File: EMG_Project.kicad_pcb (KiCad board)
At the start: 2 copper layers, 78 parts, among them J1 Conn_01x03, J10 Conn_01x01, J11 Conn_01x01, J12 Conn_01x02, J13 Conn_01x01, J14 Conn_01x01, J15 Conn_01x01, J16 Conn_01x01, J17 Conn_01x03, J2 Conn_01x06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

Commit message: First layout sketch
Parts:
- removed J13, J16, J3: Conn_01x01, Connector_PinHeader_2.54mm:PinHeader_1x01_P2.54mm_Vertical
- added J18: Conn_01x02, Connector_PinHeader_2.54mm:PinHeader_1x02_P2.54mm_Horizontal, F.Cu at (66.9, 57.1)
- added R26: 0, Resistor_SMD:R_0603_1608Metric_Pad0.98x0.95mm_HandSolder, F.Cu at (100.5, 65.2)
- U1: footprint EMG Projct Footprints:MP2322GQHZ -> EMG Projct Footprints:QFN-8_1p5MMx2MM_MNP
- moved H3 132.2 mm to (150.8, 66.0)
- moved H2 129.9 mm to (150.8, 44.1)
- moved C10 97.0 mm to (144.6, 43.5)
- moved C11 93.5 mm to (144.6, 46.5)
- moved J11 92.4 mm to (72.0, 57.0)
- moved C19 90.7 mm to (143.2, 52.0), turned to -90 degrees
- moved C20 88.3 mm to (140.0, 65.1), turned to 90 degrees
- moved C12 87.6 mm to (136.7, 57.5), turned to -90 degrees
- moved J14 86.9 mm to (85.7, 65.4)
- moved R17 82.9 mm to (143.2, 65.1), turned to -90 degrees
- moved C17 80.5 mm to (131.3, 62.4), turned to 180 degrees
- moved R16 79.8 mm to (140.7, 43.5), turned to 180 degrees
- moved R12 79.7 mm to (140.7, 46.5), turned to 180 degrees
- moved R23 79.0 mm to (143.2, 57.5), turned to -90 degrees
- moved R19 78.0 mm to (136.7, 65.1), turned to 90 degrees
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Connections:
- J1 pad 1: /REG_OUT -> +5V
- J1 pad 3: +5V -> /REG_OUT
- U2 pad 2: /V_OUT_SENSOR -> /V_IN_MCU
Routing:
- added copper zone on In2.Cu, net +3.3V
- added copper zone on In2.Cu, net /V_REF
- added copper zone on B.Cu, net GND
- added copper zone on In1.Cu, net GND
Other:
- board outline added: 97.1 x 32.3 mm
- copper layers 2 -> 4
- board text added: "+5V"
- board text added: "AAOO"
- board text added: "GND"
- board text added: "MISO"
- board text added: "MOSI"
- board text added: "Power ON"
- board text added: "R"
- board text added: "RST"
- board text added: "S"
- board text added: "SCK"
- board text added: "T"

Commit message: Everything prepared for routing
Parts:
- moved J14 2.10 mm to (85.7, 67.5), turned to 90 degrees
- moved H2 1.17 mm to (151.0, 42.9)
- moved J10 0.92 mm to (149.6, 54.8)
- moved H4 0.91 mm to (67.4, 66.0)
- moved J15 0.75 mm to (149.6, 59.7)
- moved J4 0.71 mm to (149.6, 50.0)
- moved J12 0.68 mm to (115.0, 66.7)
- moved J11 0.61 mm to (72.6, 57.1), turned to -90 degrees
- moved J9 0.21 mm to (110.8, 41.6)
- moved H1 0.20 mm to (67.4, 42.9)
- moved J8 0.20 mm to (121.3, 67.5), turned to 90 degrees
- moved J1 0.20 mm to (75.3, 65.2)
- moved H3 0.17 mm to (151.0, 66.0)
- moved J18 0.15 mm to (66.8, 57.1)
- moved J17 0.13 mm to (96.2, 42.3)
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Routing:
- net GND: track 0.00 -> 6.31 mm
- added copper zone on F.Cu, net GND
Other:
- board size 97.1 x 32.3 mm -> 93.5 x 33 mm
- board text added: "+1.5V"
- board text added: "+3.3V"
- board text added: "EMG Project version 1.0 30.04.2025"
- board text added: "Elecrode -"
- board text added: "Electrode +"
- board text added: "HP Filter"
- board text added: "INST OUT"
- board text added: "Power Select"
- board text added: "RESET"
- board text added: "SENSOR"
- board text removed: "AAOO"

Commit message: Minor layout adjustments
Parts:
- moved C20 3.31 mm to (143.3, 65.1), turned to -90 degrees
- moved R17 3.28 mm to (139.9, 65.1), turned to 90 degrees
- moved J14 0.62 mm to (85.7, 66.9)
- moved J7 0.62 mm to (106.0, 66.9)
- moved J8 0.62 mm to (121.3, 66.9)
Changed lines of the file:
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@@
 	(footprint "Connector_PinHeader_2.54mm:PinHeader_1x01_P2.54mm_Vertical"
 		(layer "F.Cu")
-		(at 121.3 67.5 90)
+		(at 121.3 66.88 90)
 		(descr "Through hole straight pin header, 1x01, 2.54mm pitch, single row")
 		(tags "Through hole pin header THT 1x01 2.54mm single row")
@@
 	(footprint "Connector_PinHeader_2.54mm:PinHeader_1x01_P2.54mm_Vertical"
 		(layer "F.Cu")
-		(at 106.05 67.5 90)
+		(at 106.05 66.88 90)
 		(descr "Through hole straight pin header, 1x01, 2.54mm pitch, single row")
 		(tags "Through hole pin header THT 1x01 2.54mm single row")
@@
 	(footprint "Connector_PinHeader_2.54mm:PinHeader_1x01_P2.54mm_Vertical"
 		(layer "F.Cu")
-		(at 85.65 67.5 90)
+		(at 85.66 66.88 90)
 		(descr "Through hole straight pin header, 1x01, 2.54mm pitch, single row")
 		(tags "Through hole pin header THT 1x01 2.54mm single row")
@@
 	(footprint "Resistor_SMD:R_0603_1608Metric_Pad0.98x0.95mm_HandSolder"
 		(layer "F.Cu")
-		(at 143.23 65.115 -90)
+		(at 139.95 65.1175 90)
 		(descr "Resistor SMD 0603 (1608 Metric), square (rectangular) end terminal, IPC-7351 nominal with elongated pad for handsoldering. (Body size source: IPC-SM-782 page 72, https://www.pcb-3d.com/wordpress/wp-content/uploads/ipc-sm-782a_amendment_1_and_2.pdf), generated with kicad-footprint-generator")
 		(tags "resistor handsolder")
 		(property "Reference" "R17"
-			(at 2.485 0.03 180)
+			(at -2.4825 0.01 0)
 			(layer "F.SilkS")
 			(effects
@@
 		)
 		(property "Comments" ""
-			(at 0 0 270)
+			(at 0 0 90)
 			(unlocked yes)
 			(layer "F.Fab")
@@
 		(attr smd)
 		(fp_line
-			(start -0.254724 0.5225)
-			(end 0.254724 0.5225)
+			(start -0.254724 -0.5225)
+			(end 0.254724 -0.5225)
 			(stroke
 				(width 0.12)
@@
 		)
 		(fp_line
-			(start -0.254724 -0.5225)
-			(end 0.254724 -0.5225)
+			(start -0.254724 0.5225)
+			(end 0.254724 0.5225)
 			(stroke
 				(width 0.12)
@@
 		)
 		(fp_line
-			(start -1.65 0.73)
-			(end -1.65 -0.73)
+			(start 1.65 -0.73)
+			(end 1.65 0.73)
 			(stroke
 				(width 0.05)
@@
 		)
 		(fp_line
-			(start 1.65 0.73)
-			(end -1.65 0.73)
+			(start -1.65 -0.73)
+			(end 1.65 -0.73)
 			(stroke
 				(width 0.05)
@@
 		)
 		(fp_line
-			(start -1.65 -0.73)
-			(end 1.65 -0.73)
+			(start 1.65 0.73)
+			(end -1.65 0.73)
 			(stroke
 				(width 0.05)
@@
 		)
 		(fp_line
-			(start 1.65 -0.73)
-			(end 1.65 0.73)
+			(start -1.65 0.73)
+			(end -1.65 -0.73)
 			(stroke
 				(width 0.05)
@@
 		)
 		(fp_line
-			(start -0.8 0.4125)
-			(end -0.8 -0.4125)
+			(start 0.8 -0.4125)
+			(end 0.8 0.4125)
 			(stroke
 				(width 0.1)
@@
 		)
 		(fp_line
-			(start 0.8 0.4125)
-			(end -0.8 0.4125)
+			(start -0.8 -0.4125)
+			(end 0.8 -0.4125)
 			(stroke
 				(width 0.1)
@@
 		)
 		(fp_line
-			(start -0.8 -0.4125)
-			(end 0.8 -0.4125)
+			(start 0.8 0.4125)
+			(end -0.8 0.4125)
 			(stroke
 				(width 0.1)
@@
 		)
 		(fp_line
-			(start 0.8 -0.4125)
-			(end 0.8 0.4125)
+			(start -0.8 0.4125)
+			(end -0.8 -0.4125)
 			(stroke
 				(width 0.1)
@@
 		)
 		(pad "1" smd roundrect
-			(at -0.9125 0 270)
+			(at -0.9125 0 90)
 			(size 0.975 0.95)
 			(layers "F.Cu" "F.Mask" "F.Paste")
@@
 		)
 		(pad "2" smd roundrect
-			(at 0.9125 0 270)
+			(at 0.9125 0 90)
 			(size 0.975 0.95)
 			(layers "F.Cu" "F.Mask" "F.Paste")
@@
 		)
 		(property "Value" "Conn_01x01"
-			(at 0 2.38 90)
+			(at -0.3 2.3 90)
 			(layer "F.Fab")
 			(effects
@@
 	(footprint "Capacitor_SMD:C_0603_1608Metric_Pad1.08x0.95mm_HandSolder"
 		(layer "F.Cu")
-		(at 139.953333 65.115 90)
+		(at 143.26 65.1375 -90)
 		(descr "Capacitor SMD 0603 (1608 Metric), square (rectangular) end terminal, IPC-7351 nominal with elongated pad for handsoldering. (Body size source: IPC-SM-782 page 76, https://www.pcb-3d.com/wordpress/wp-content/uploads/ipc-sm-782a_amendment_1_and_2.pdf), generated with kicad-footprint-generator")
 		(tags "capacitor handsolder")
 		(property "Reference" "C20"
-			(at -2.485 0.046667 180)
+			(at 2.4625 0 0)
 			(layer "F.SilkS")
 			(effects
@@
 		)
 		(property "Comments" ""
-			(at 0 0 90)
+			(at 0 0 270)
 			(unlocked yes)
 			(layer "F.Fab")
@@
 		(attr smd)
 		(fp_line
-			(start -0.146267 -0.51)
-			(end 0.146267 -0.51)
+			(start -0.146267 0.51)
+			(end 0.146267 0.51)
 			(stroke
 				(width 0.12)
@@
 		)
 		(fp_line
-			(start -0.146267 0.51)
-			(end 0.146267 0.51)
+			(start -0.146267 -0.51)
+			(end 0.146267 -0.51)
 			(stroke
 				(width 0.12)
@@
 		)
 		(fp_line
-			(start 1.65 -0.73)
-			(end 1.65 0.73)
+			(start -1.65 0.73)
+			(end -1.65 -0.73)
 			(stroke
 				(width 0.05)
@@
 		)
 		(fp_line
-			(start -1.65 -0.73)
-			(end 1.65 -0.73)
+			(start 1.65 0.73)
+			(end -1.65 0.73)
 			(stroke
 				(width 0.05)
@@
 		)
 		(fp_line
-			(start 1.65 0.73)
-			(end -1.65 0.73)
+			(start -1.65 -0.73)
+			(end 1.65 -0.73)
 			(stroke
 				(width 0.05)
@@
 		)
 		(fp_line
-			(start -1.65 0.73)
-			(end -1.65 -0.73)
+			(start 1.65 -0.73)
+			(end 1.65 0.73)
 			(stroke
 				(width 0.05)
@@
 		)
 		(fp_line
-			(start 0.8 -0.4)
-			(end 0.8 0.4)
+			(start -0.8 0.4)
+			(end -0.8 -0.4)
 			(stroke
 				(width 0.1)
@@
 		)
 		(fp_line
-			(start -0.8 -0.4)
-			(end 0.8 -0.4)
+			(start 0.8 0.4)
+			(end -0.8 0.4)
 			(stroke
 				(width 0.1)
@@
 		)
 		(fp_line
-			(start 0.8 0.4)
-			(end -0.8 0.4)
+			(start -0.8 -0.4)
+			(end 0.8 -0.4)
 			(stroke
 				(width 0.1)
@@
 		)
 		(fp_line
-			(start -0.8 0.4)
-			(end -0.8 -0.4)
+			(start 0.8 -0.4)
+			(end 0.8 0.4)
 			(stroke
 				(width 0.1)
@@
 		)
 		(pad "1" smd roundrect
-			(at -0.8625 0 90)
+			(at -0.8625 0 270)
 			(size 1.075 0.95)
 			(layers "F.Cu" "F.Mask" "F.Paste")
@@
 		)
 		(pad "2" smd roundrect
-			(at 0.8625 0 90)
+			(at 0.8625 0 270)
 			(size 1.075 0.95)
 			(layers "F.Cu" "F.Mask" "F.Paste")
@@
 		(model "${KIPRJMOD}/Libraries/3D Models/SJ1-3523N.step"
 			(offset
-				(xyz 0 -7 3.5)
+				(xyz 0 -7 2.5)
 			)
 			(scale
@@
 	)
 	(gr_text "GND"
-		(at 119.75 70.61 0)
+		(at 119.75 70.01 0)
 		(layer "F.SilkS")
 		(effects
@@
 	)
 	(gr_text "GND"
-		(at 84.076191 70.61 0)
+		(at 84.086191 70.01 0)
 		(layer "F.SilkS")
 		(effects
@@
 	)
 	(gr_text "GND"
-		(at 104.476191 70.61 0)
+		(at 104.476191 70.01 0)
 		(layer "F.SilkS")
 		(effects

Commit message: Routing of version 1 complete
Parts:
- moved R17 3.36 mm to (143.3, 65.1)
- moved C20 3.27 mm to (140.0, 65.1)
- turned C4 to 90 degrees
- turned R3 to 90 degrees
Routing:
- net +5V: track 0.00 -> 45.3 mm, vias 0 -> 3
- net /RST: track 0.00 -> 43.3 mm, vias 0 -> 4
- net /V_OUT_SENSOR: track 0.00 -> 40.8 mm
- net /V_REF: track 0.00 -> 29.4 mm, vias 0 -> 10
- net /V_OUT_INST: track 0.00 -> 27.5 mm, vias 0 -> 2
- net /V_IN_INST_N: track 0.00 -> 27.1 mm
- net Net-(U3-REF): track 0.00 -> 26.9 mm
- net /T: track 0.00 -> 26.5 mm
- net +3.3V: track 0.00 -> 25.5 mm, vias 0 -> 10
- net /V_IN_INST_P: track 0.00 -> 25.5 mm
- net /REG_OUT: track 0.00 -> 23.4 mm
- net /R: track 0.00 -> 23.3 mm
- net /SCK: track 0.00 -> 23.1 mm
- net /MISO: track 0.00 -> 22.0 mm
- net /S: track 0.00 -> 20.8 mm
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- added copper zone on F.Cu, net +5V

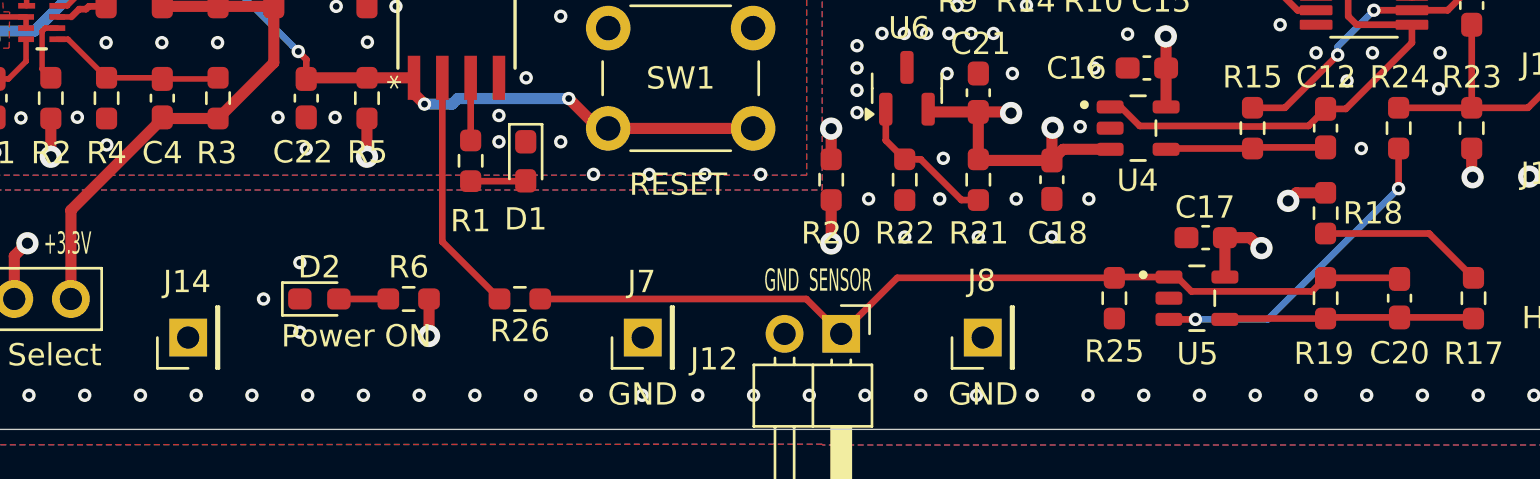
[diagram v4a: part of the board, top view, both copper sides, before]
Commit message: Minor grounding changes and gerber files
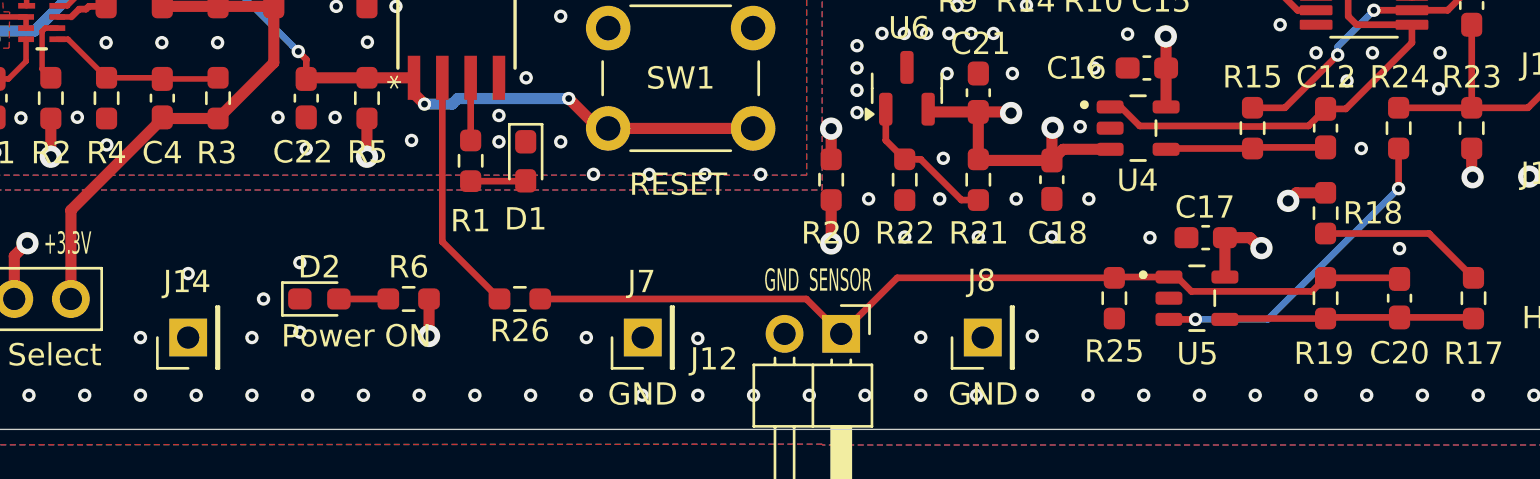
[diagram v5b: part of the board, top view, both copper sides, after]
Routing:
- net GND: vias 179 -> 189
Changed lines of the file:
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@@
+	)
+	(via
+		(at 83.52 66.88)
+		(size 0.6)
+		(drill 0.3)
+		(layers "F.Cu" "B.Cu")
+		(free yes)
+		(net 1)
 	)
 	(via
@@
 	)
 	(via
+		(at 123.52 66.81)
+		(size 0.6)
+		(drill 0.3)
+		(layers "F.Cu" "B.Cu")
+		(free yes)
+		(net 1)
+	)
+	(via
 		(at 84.97 44.56)
 		(size 0.6)
@@
 	)
 	(via
+		(at 118.52 66.87)
+		(size 0.6)
+		(drill 0.3)
+		(layers "F.Cu" "B.Cu")
+		(free yes)
+		(net 1)
+	)
+	(via
 		(at 118.56 39.25)
 		(size 0.6)
@@
 	)
 	(via
+		(at 108.52 66.92)
+		(size 0.6)
+		(drill 0.3)
+		(layers "F.Cu" "B.Cu")
+		(free yes)
+		(net 1)
+	)
+	(via
 		(at 89.69 57.004999)
 		(size 0.6)
@@
 	)
 	(via
+		(at 95.68 58.04)
+		(size 0.6)
+		(drill 0.3)
+		(layers "F.Cu" "B.Cu")
+		(free yes)
+		(net 1)
+	)
+	(via
 		(at 98.56 39.25)
 		(size 0.6)
@@
 	)
 	(via
+		(at 128.8 62.4)
+		(size 0.6)
+		(drill 0.3)
+		(layers "F.Cu" "B.Cu")
+		(free yes)
+		(net 1)
+	)
+	(via
 		(at 74.62 48.82)
 		(size 0.6)
@@
 	)
 	(via
+		(at 139.993334 62.89)
+		(size 0.6)
+		(drill 0.3)
+		(layers "F.Cu" "B.Cu")
+		(free yes)
+		(net 1)
+	)
+	(via
 		(at 91.02 69.4705)
 		(size 0.6)
@@
 	)
 	(via
+		(at 85.66 64.01)
+		(size 0.6)
+		(drill 0.3)
+		(layers "F.Cu" "B.Cu")
+		(free yes)
+		(net 1)
+	)
+	(via
 		(at 82.01 58.24)
 		(size 0.6)
@@
 	)
 	(via
+		(at 88.52 66.88)
+		(size 0.6)
+		(drill 0.3)
+		(layers "F.Cu" "B.Cu")
+		(free yes)
+		(net 1)
+	)
+	(via
 		(at 64.32 54.6)
 		(size 0.6)
@@
 		(size 0.6)
 		(drill 0.3)
+		(layers "F.Cu" "B.Cu")
+		(free yes)
+		(net 1)
+	)
+	(via
+		(at 103.52 66.88)
+		(size 0.6)
+		(drill 0.3)
